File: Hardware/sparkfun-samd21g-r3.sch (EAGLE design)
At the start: 60 parts, among them Q1 2.5A/30V, Q2 2N7002PW, U1 MCP73831, U2 74AHC1G125, U3 MIC5219 3.3V, U4 ATSAMD21G-A, Y1 32.768kHz

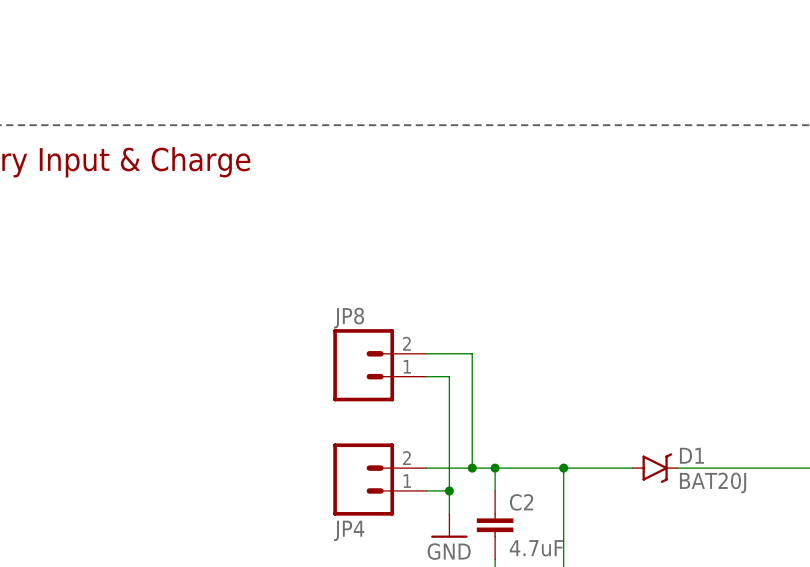
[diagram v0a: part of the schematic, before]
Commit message: Renaming files and board name silk.
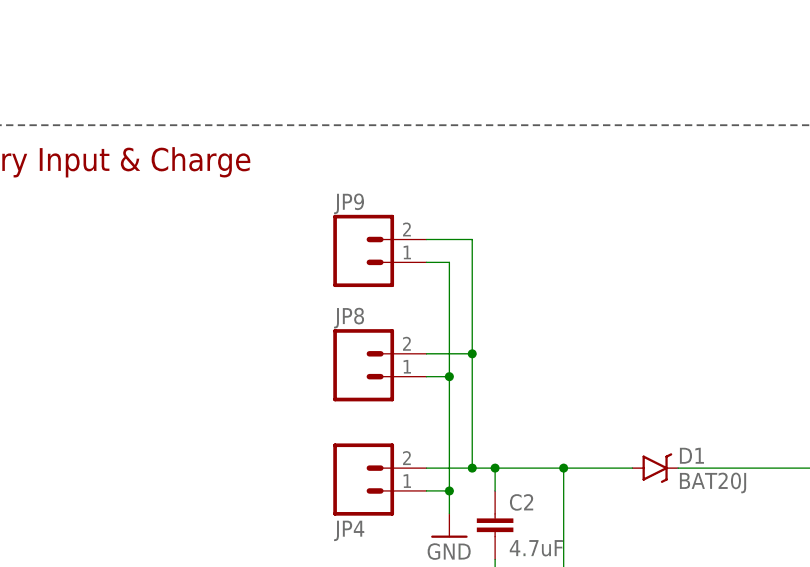
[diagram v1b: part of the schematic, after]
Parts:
- added JP9: (no value), SparkFun-Connectors:M021X02_NO_SILK
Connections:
- net GND: now also JP9.1
- net VBAT: now also JP9.2
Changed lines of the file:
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@@
 <part name="SUPPLY19" library="SparkFun-Aesthetics" deviceset="VIN" device=""/>
 <part name="JP8" library="SparkFun-Connectors" deviceset="M02" device="-JST-2-PTH-NO_SILK"/>
+<part name="JP9" library="SparkFun-Connectors" deviceset="M02" device="1X02_NO_SILK"/>
 </parts>
 <sheets>
@@
 <instance part="SUPPLY19" gate="G$1" x="172.72" y="251.46"/>
 <instance part="JP8" gate="G$1" x="50.8" y="154.94"/>
+<instance part="JP9" gate="G$1" x="50.8" y="167.64"/>
 </instances>
 <busses>
@@
 <pinref part="JP8" gate="G$1" pin="1"/>
 <wire x1="58.42" y1="154.94" x2="60.96" y2="154.94" width="0.1524" layer="91"/>
+<pinref part="JP9" gate="G$1" pin="1"/>
+<wire x1="58.42" y1="167.64" x2="60.96" y2="167.64" width="0.1524" layer="91"/>
+<wire x1="60.96" y1="167.64" x2="60.96" y2="154.94" width="0.1524" layer="91"/>
+<junction x="60.96" y="154.94"/>
 </segment>
 <segment>
@@
 <pinref part="JP8" gate="G$1" pin="2"/>
 <wire x1="58.42" y1="157.48" x2="63.5" y2="157.48" width="0.1524" layer="91"/>
-</segment>
-</net>
+<pinref part="JP9" gate="G$1" pin="2"/>
+<wire x1="58.42" y1="170.18" x2="63.5" y2="170.18" width="0.1524" layer="91"/>
+<wire x1="63.5" y1="170.18" x2="63.5" y2="157.48" width="0.1524" layer="91"/>
+<junction x="63.5" y="157.48"/>
+</segment>
+</net>

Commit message: Adding PROD_ID to L1.
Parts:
- L1: PROD_ID (none) -> RES-07859
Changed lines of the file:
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@@
 <grid distance="0.1" unitdist="inch" unit="inch" style="lines" multiple="1" display="no" altdistance="0.01" altunitdist="inch" altunit="inch"/>
 <layers>
-<layer number="1" name="Top" color="4" fill="1" visible="yes" active="no"/>
-<layer number="2" name="Route2" color="1" fill="3" visible="yes" active="no"/>
-<layer number="3" name="Route3" color="4" fill="3" visible="yes" active="no"/>
-<layer number="4" name="Route4" color="1" fill="4" visible="yes" active="no"/>
-<layer number="5" name="Route5" color="4" fill="4" visible="yes" active="no"/>
-<layer number="6" name="Route6" color="1" fill="8" visible="yes" active="no"/>
-<layer number="7" name="Route7" color="4" fill="8" visible="yes" active="no"/>
-<layer number="8" name="Route8" color="1" fill="2" visible="yes" active="no"/>
-<layer number="9" name="Route9" color="4" fill="2" visible="yes" active="no"/>
-<layer number="10" name="Route10" color="1" fill="7" visible="yes" active="no"/>
-<layer number="11" name="Route11" color="4" fill="7" visible="yes" active="no"/>
-<layer number="12" name="Route12" color="1" fill="5" visible="yes" active="no"/>
-<layer number="13" name="Route13" color="4" fill="5" visible="yes" active="no"/>
-<layer number="14" name="Route14" color="1" fill="6" visible="yes" active="no"/>
-<layer number="15" name="Route15" color="4" fill="6" visible="yes" active="no"/>
-<layer number="16" name="Bottom" color="1" fill="1" visible="yes" active="no"/>
-<layer number="17" name="Pads" color="2" fill="1" visible="yes" active="no"/>
-<layer number="18" name="Vias" color="2" fill="1" visible="yes" active="no"/>
-<layer number="19" name="Unrouted" color="6" fill="1" visible="yes" active="no"/>
-<layer number="20" name="Dimension" color="15" fill="1" visible="yes" active="no"/>
-<layer number="21" name="tPlace" color="16" fill="1" visible="yes" active="no"/>
-<layer number="22" name="bPlace" color="14" fill="1" visible="yes" active="no"/>
-<layer number="23" name="tOrigins" color="15" fill="1" visible="yes" active="no"/>
-<layer number="24" name="bOrigins" color="15" fill="1" visible="yes" active="no"/>
-<layer number="25" name="tNames" color="7" fill="1" visible="yes" active="no"/>
-<layer number="26" name="bNames" color="7" fill="1" visible="yes" active="no"/>
-<layer number="27" name="tValues" color="7" fill="1" visible="yes" active="no"/>
-<layer number="28" name="bValues" color="7" fill="1" visible="yes" active="no"/>
+<layer number="1" name="Top" color="4" fill="1" visible="no" active="no"/>
+<layer number="2" name="Route2" color="1" fill="3" visible="no" active="no"/>
+<layer number="3" name="Route3" color="4" fill="3" visible="no" active="no"/>
+<layer number="4" name="Route4" color="1" fill="4" visible="no" active="no"/>
+<layer number="5" name="Route5" color="4" fill="4" visible="no" active="no"/>
+<layer number="6" name="Route6" color="1" fill="8" visible="no" active="no"/>
+<layer number="7" name="Route7" color="4" fill="8" visible="no" active="no"/>
+<layer number="8" name="Route8" color="1" fill="2" visible="no" active="no"/>
+<layer number="9" name="Route9" color="4" fill="2" visible="no" active="no"/>
+<layer number="10" name="Route10" color="1" fill="7" visible="no" active="no"/>
+<layer number="11" name="Route11" color="4" fill="7" visible="no" active="no"/>
+<layer number="12" name="Route12" color="1" fill="5" visible="no" active="no"/>
+<layer number="13" name="Route13" color="4" fill="5" visible="no" active="no"/>
+<layer number="14" name="Route14" color="1" fill="6" visible="no" active="no"/>
+<layer number="15" name="Route15" color="4" fill="6" visible="no" active="no"/>
+<layer number="16" name="Bottom" color="1" fill="1" visible="no" active="no"/>
+<layer number="17" name="Pads" color="2" fill="1" visible="no" active="no"/>
+<layer number="18" name="Vias" color="2" fill="1" visible="no" active="no"/>
+<layer number="19" name="Unrouted" color="6" fill="1" visible="no" active="no"/>
+<layer number="20" name="Dimension" color="15" fill="1" visible="no" active="no"/>
+<layer number="21" name="tPlace" color="16" fill="1" visible="no" active="no"/>
+<layer number="22" name="bPlace" color="14" fill="1" visible="no" active="no"/>
+<layer number="23" name="tOrigins" color="15" fill="1" visible="no" active="no"/>
+<layer number="24" name="bOrigins" color="15" fill="1" visible="no" active="no"/>
+<layer number="25" name="tNames" color="7" fill="1" visible="no" active="no"/>
+<layer number="26" name="bNames" color="7" fill="1" visible="no" active="no"/>
+<layer number="27" name="tValues" color="7" fill="1" visible="no" active="no"/>
+<layer number="28" name="bValues" color="7" fill="1" visible="no" active="no"/>
 <layer number="29" name="tStop" color="7" fill="6" visible="no" active="no"/>
 <layer number="30" name="bStop" color="7" fill="3" visible="no" active="no"/>
@@
 <layer number="35" name="tGlue" color="7" fill="4" visible="no" active="no"/>
 <layer number="36" name="bGlue" color="7" fill="5" visible="no" active="no"/>
-<layer number="37" name="tTest" color="7" fill="1" visible="yes" active="no"/>
-<layer number="38" name="bTest" color="7" fill="1" visible="yes" active="no"/>
+<layer number="37" name="tTest" color="7" fill="1" visible="no" active="no"/>
+<layer number="38" name="bTest" color="7" fill="1" visible="no" active="no"/>
 <layer number="39" name="tKeepout" color="4" fill="11" visible="no" active="no"/>
 <layer number="40" name="bKeepout" color="1" fill="11" visible="no" active="no"/>
@@
 <layer number="44" name="Drills" color="7" fill="1" visible="no" active="no"/>
 <layer number="45" name="Holes" color="7" fill="1" visible="no" active="no"/>
-<layer number="46" name="Milling" color="3" fill="1" visible="yes" active="no"/>
-<layer number="47" name="Measures" color="7" fill="1" visible="yes" active="no"/>
-<layer number="48" name="Document" color="7" fill="1" visible="yes" active="no"/>
-<layer number="49" name="Reference" color="7" fill="1" visible="yes" active="no"/>
-<layer number="50" name="dxf" color="7" fill="1" visible="yes" active="no"/>
-<layer number="51" name="tDocu" color="6" fill="1" visible="yes" active="no"/>
-<layer number="52" name="bDocu" color="6" fill="1" visible="yes" active="no"/>
-<layer number="53" name="tGND_GNDA" color="7" fill="9" visible="yes" active="no"/>
-<layer number="54" name="bGND_GNDA" color="1" fill="9" visible="yes" active="no"/>
-<layer number="56" name="wert" color="7" fill="1" visible="yes" active="no"/>
-<layer number="57" name="tCAD" color="7" fill="1" visible="yes" active="no"/>
-<layer number="59" name="tCarbon" color="7" fill="1" visible="yes" active="no"/>
-<layer number="60" name="bCarbon" color="7" fill="1" visible="yes" active="no"/>
+<layer number="46" name="Milling" color="3" fill="1" visible="no" active="no"/>
+<layer number="47" name="Measures" color="7" fill="1" visible="no" active="no"/>
+<layer number="48" name="Document" color="7" fill="1" visible="no" active="no"/>
+<layer number="49" name="Reference" color="7" fill="1" visible="no" active="no"/>
+<layer number="50" name="dxf" color="7" fill="1" visible="no" active="no"/>
+<layer number="51" name="tDocu" color="6" fill="1" visible="no" active="no"/>
+<layer number="52" name="bDocu" color="6" fill="1" visible="no" active="no"/>
+<layer number="53" name="tGND_GNDA" color="7" fill="9" visible="no" active="no"/>
+<layer number="54" name="bGND_GNDA" color="1" fill="9" visible="no" active="no"/>
+<layer number="56" name="wert" color="7" fill="1" visible="no" active="no"/>
+<layer number="57" name="tCAD" color="7" fill="1" visible="no" active="no"/>
+<layer number="59" name="tCarbon" color="7" fill="1" visible="no" active="no"/>
+<layer number="60" name="bCarbon" color="7" fill="1" visible="no" active="no"/>
 <layer number="90" name="Modules" color="5" fill="1" visible="yes" active="yes"/>
 <layer number="91" name="Nets" color="2" fill="1" visible="yes" active="yes"/>
@@
 <part name="GND21" library="SparkFun-Aesthetics" deviceset="GND" device=""/>
 <part name="GND23" library="SparkFun-Aesthetics" deviceset="GND" device=""/>
-<part name="L1" library="SparkFun-Passives" deviceset="INDUCTOR" device="0603" value="FB - 30Ohm"/>
+<part name="L1" library="SparkFun-Passives" deviceset="INDUCTOR" device="0603" value="FB - 30Ohm">
+<attribute name="PROD_ID" value="RES-07859"/>
+</part>
 <part name="GND19" library="SparkFun-Aesthetics" deviceset="GND" device=""/>
 <part name="SUPPLY12" library="SparkFun-Aesthetics" deviceset="3.3V" device=""/>
@@
 <attribute name="NAME" x="281.94" y="241.3" size="1.778" layer="95"/>
 <attribute name="VALUE" x="278.384" y="228.6" size="1.778" layer="96" rot="R90"/>
+<attribute name="PROD_ID" x="279.4" y="236.22" size="1.27" layer="96" display="off"/>
 </instance>
 <instance part="GND19" gate="1" x="279.4" y="210.82"/>

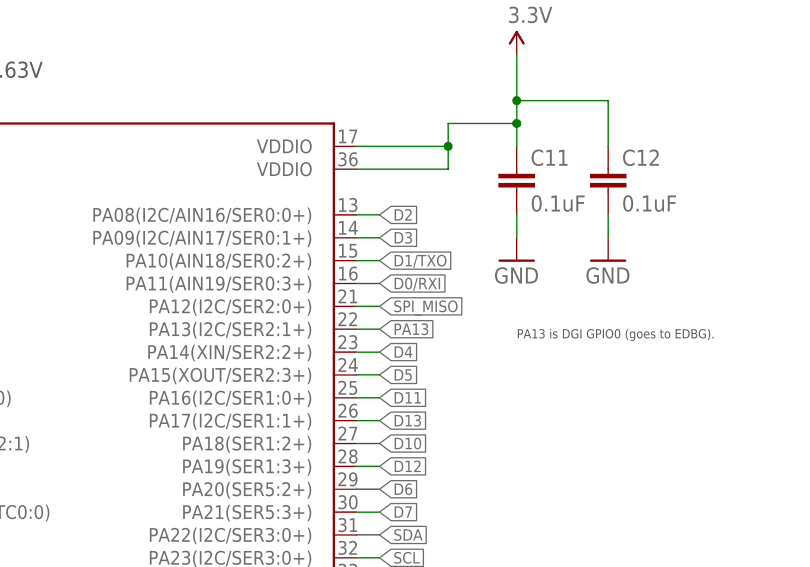
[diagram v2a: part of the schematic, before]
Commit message: Swapping D2 and D4.
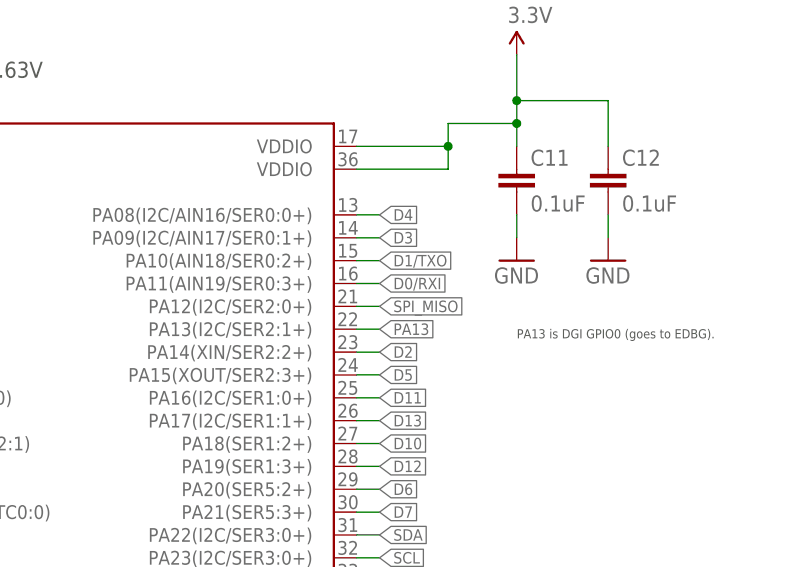
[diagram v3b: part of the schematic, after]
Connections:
- net D2: now also U4.PA14(XIN/SER2:2+); no longer U4.PA08(I2C/AIN16/SER0:0+)
- net D4: now also U4.PA08(I2C/AIN16/SER0:0+); no longer U4.PA14(XIN/SER2:2+)
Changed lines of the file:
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@@
 </segment>
 </net>
-<net name="D2" class="0">
+<net name="D4" class="0">
 <segment>
 <pinref part="U4" gate="G$1" pin="PA08(I2C/AIN16/SER0:0+)"/>
@@
 </segment>
 <segment>
-<pinref part="JP7" gate="G$1" pin="D2"/>
-<wire x1="215.9" y1="111.76" x2="218.44" y2="111.76" width="0.1524" layer="91"/>
-<label x="218.44" y="111.76" size="1.27" layer="95" xref="yes"/>
+<pinref part="JP7" gate="G$1" pin="D4"/>
+<wire x1="215.9" y1="106.68" x2="218.44" y2="106.68" width="0.1524" layer="91"/>
+<label x="218.44" y="106.68" size="1.27" layer="95" xref="yes"/>
 </segment>
 </net>
@@
 </segment>
 </net>
-<net name="D4" class="0">
+<net name="D2" class="0">
 <segment>
 <pinref part="U4" gate="G$1" pin="PA14(XIN/SER2:2+)"/>
@@
 </segment>
 <segment>
-<pinref part="JP7" gate="G$1" pin="D4"/>
-<wire x1="215.9" y1="106.68" x2="218.44" y2="106.68" width="0.1524" layer="91"/>
-<label x="218.44" y="106.68" size="1.27" layer="95" xref="yes"/>
+<pinref part="JP7" gate="G$1" pin="D2"/>
+<wire x1="215.9" y1="111.76" x2="218.44" y2="111.76" width="0.1524" layer="91"/>
+<label x="218.44" y="111.76" size="1.27" layer="95" xref="yes"/>
 </segment>
 </net>

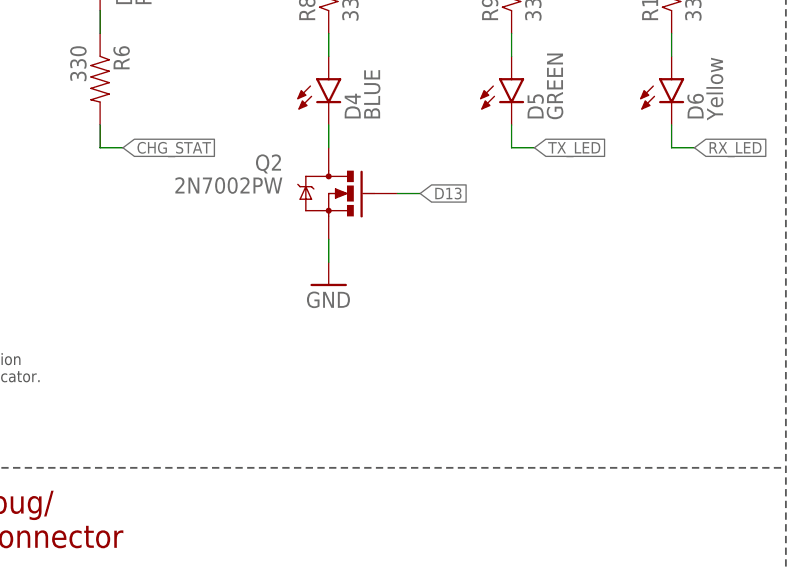
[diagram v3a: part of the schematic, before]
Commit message: Adding pull-down resistor to D13 LED/MOSFET
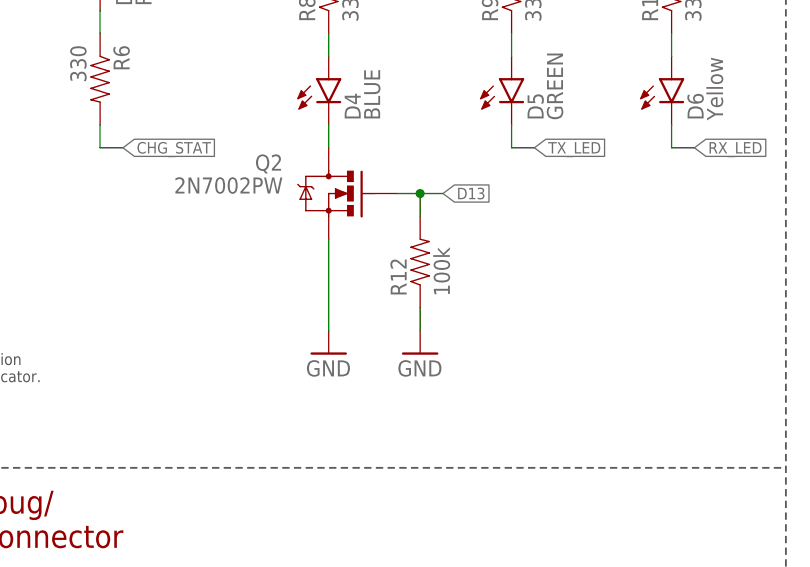
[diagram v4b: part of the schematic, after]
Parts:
- added R12: 100k, SparkFun-Resistors:100KOHM-1/10W-1%(0603)
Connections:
- net D13: now also R12.2
- net GND: now also R12.1
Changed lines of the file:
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@@
 <part name="JP8" library="SparkFun-Connectors" deviceset="M02" device="-JST-2-PTH-NO_SILK"/>
 <part name="JP9" library="SparkFun-Connectors" deviceset="M02" device="1X02_NO_SILK"/>
+<part name="R12" library="SparkFun-Resistors" deviceset="100KOHM-1/10W-1%(0603)" device="" value="100k"/>
+<part name="GND27" library="SparkFun-Aesthetics" deviceset="GND" device=""/>
 </parts>
 <sheets>
@@
 <instance part="SUPPLY7" gate="G$1" x="152.4" y="251.46"/>
 <instance part="GND14" gate="1" x="152.4" y="210.82"/>
-<instance part="GND17" gate="1" x="198.12" y="210.82"/>
+<instance part="GND17" gate="1" x="198.12" y="203.2"/>
 <instance part="D4" gate="G$1" x="198.12" y="233.68"/>
 <instance part="C3" gate="G$1" x="99.06" y="218.44" rot="MR0"/>
@@
 <instance part="JP8" gate="G$1" x="50.8" y="154.94"/>
 <instance part="JP9" gate="G$1" x="50.8" y="167.64"/>
+<instance part="R12" gate="G$1" x="208.28" y="213.36" rot="R90"/>
+<instance part="GND27" gate="1" x="208.28" y="203.2"/>
 </instances>
 <busses>
@@
 <pinref part="GND17" gate="1" pin="GND"/>
 <pinref part="Q2" gate="G$1" pin="S"/>
-<wire x1="198.12" y1="213.36" x2="198.12" y2="215.9" width="0.1524" layer="91"/>
+<wire x1="198.12" y1="205.74" x2="198.12" y2="215.9" width="0.1524" layer="91"/>
 </segment>
 <segment>
@@
 <pinref part="GND2" gate="1" pin="GND"/>
 <wire x1="30.48" y1="261.62" x2="30.48" y2="259.08" width="0.1524" layer="91"/>
+</segment>
+<segment>
+<pinref part="R12" gate="G$1" pin="1"/>
+<pinref part="GND27" gate="1" pin="GND"/>
+<wire x1="208.28" y1="205.74" x2="208.28" y2="208.28" width="0.1524" layer="91"/>
 </segment>
 </net>
@@
 <pinref part="Q2" gate="G$1" pin="G"/>
 <wire x1="205.74" y1="220.98" x2="208.28" y2="220.98" width="0.1524" layer="91"/>
-<label x="208.28" y="220.98" size="1.27" layer="95" xref="yes"/>
-</segment>
-</net>
+<label x="210.82" y="220.98" size="1.27" layer="95" xref="yes"/>
+<pinref part="R12" gate="G$1" pin="2"/>
+<wire x1="208.28" y1="220.98" x2="210.82" y2="220.98" width="0.1524" layer="91"/>
+<wire x1="208.28" y1="218.44" x2="208.28" y2="220.98" width="0.1524" layer="91"/>
+<junction x="208.28" y="220.98"/>
+</segment>
+</net>

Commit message: Upping version number to v10
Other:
- note added: "v10"
- note removed: "v01"
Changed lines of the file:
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@@
 <text x="251.46" y="276.86" size="2.54" layer="94" align="top-left">ATSAMD21G</text>
 <text x="353.06" y="10.16" size="2.54" layer="94" align="top-left">Jim Lindblom</text>
-<text x="421.64" y="10.16" size="2.54" layer="94" align="top-left">v01</text>
+<text x="421.64" y="10.16" size="2.54" layer="94" align="top-left">v10</text>
 <wire x1="248.92" y1="0" x2="248.92" y2="35.56" width="0.2032" layer="97" style="longdash"/>
 <text x="2.54" y="53.34" size="2.54" layer="94" align="top-left">USB Host/Device Control</text>
